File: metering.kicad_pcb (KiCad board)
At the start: 2 copper layers, 75 x 86 mm, 61 parts, among them J1 Conn_01x08, J2 USB_C_Receptacle_USB2.0_16P, J3 Prog, P1 Conn_01x08, SW1 Reset, SW2 Boot, U1 USBLC6-2SC6, U2 AMS1117-3.3, U3 ESP32-C3-WROOM-02U, U4 74HC14, X1 Screw_Terminal_01x06, X2 Screw_Terminal_01x06, Y1 32.768kHz

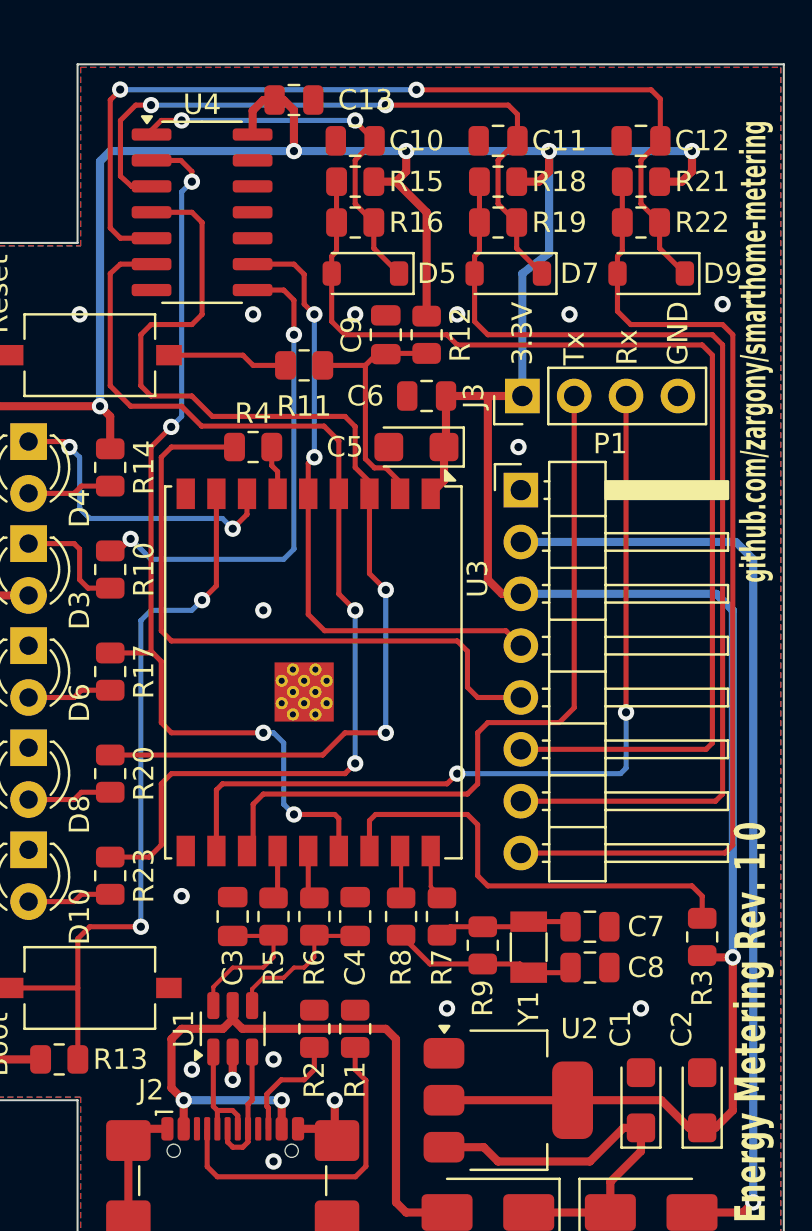
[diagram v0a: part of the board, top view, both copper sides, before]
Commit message: Add more GND vias
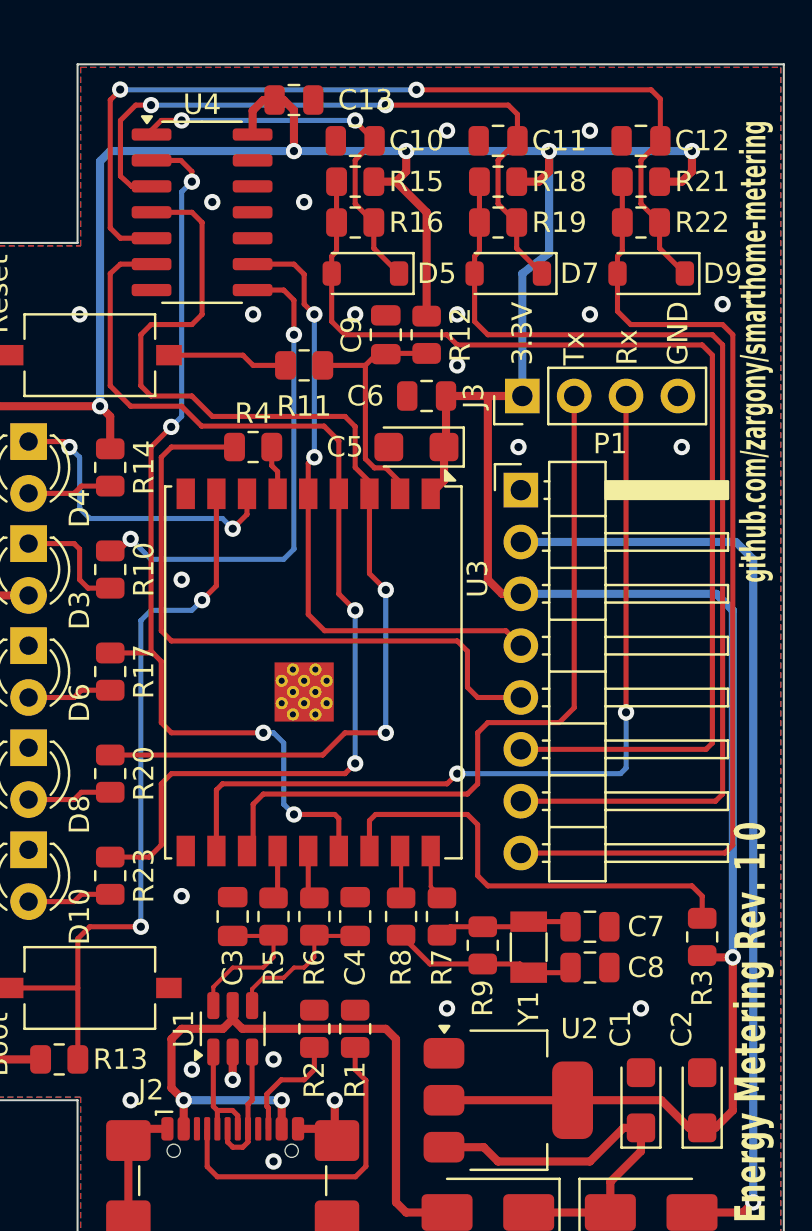
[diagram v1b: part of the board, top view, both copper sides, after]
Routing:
- net GND: vias 16 -> 23
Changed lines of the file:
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@@
+	)
+	(via
+		(at 49.5 121)
+		(size 0.8)
+		(drill 0.4)
+		(layers "F.Cu" "B.Cu")
+		(free yes)
+		(net 1)
+	)
+	(via
+		(at 65.5 85)
+		(size 0.8)
+		(drill 0.4)
+		(layers "F.Cu" "B.Cu")
+		(free yes)
+		(net 1)
 	)
 	(via
@@
 	)
 	(via
+		(at 65 73.5)
+		(size 0.8)
+		(drill 0.4)
+		(layers "F.Cu" "B.Cu")
+		(free yes)
+		(net 1)
+	)
+	(via
 		(at 52.5 119.5)
+		(size 0.8)
+		(drill 0.4)
+		(layers "F.Cu" "B.Cu")
+		(free yes)
+		(net 1)
+	)
+	(via
+		(at 53.5 77)
 		(size 0.8)
 		(drill 0.4)
@@
 	)
 	(via
-		(at 56 97)
+		(at 52 95.5)
 		(size 0.8)
 		(drill 0.4)
@@
 	)
 	(via
-		(at 71 82.5)
+		(at 72 82.5)
+		(size 0.8)
+		(drill 0.4)
+		(layers "F.Cu" "B.Cu")
+		(free yes)
+		(net 1)
+	)
+	(via
+		(at 58 77)
 		(size 0.8)
 		(drill 0.4)
@@
 	(via
 		(at 65 116.5)
+		(size 0.8)
+		(drill 0.4)
+		(layers "F.Cu" "B.Cu")
+		(free yes)
+		(net 1)
+	)
+	(via
+		(at 72 73.5)
 		(size 0.8)
 		(drill 0.4)
@@
 		(size 0.8)
 		(drill 0.4)
+		(layers "F.Cu" "B.Cu")
+		(free yes)
+		(net 1)
+	)
+	(via
+		(at 76.5 89)
+		(size 0.8)
+		(drill 0.4)

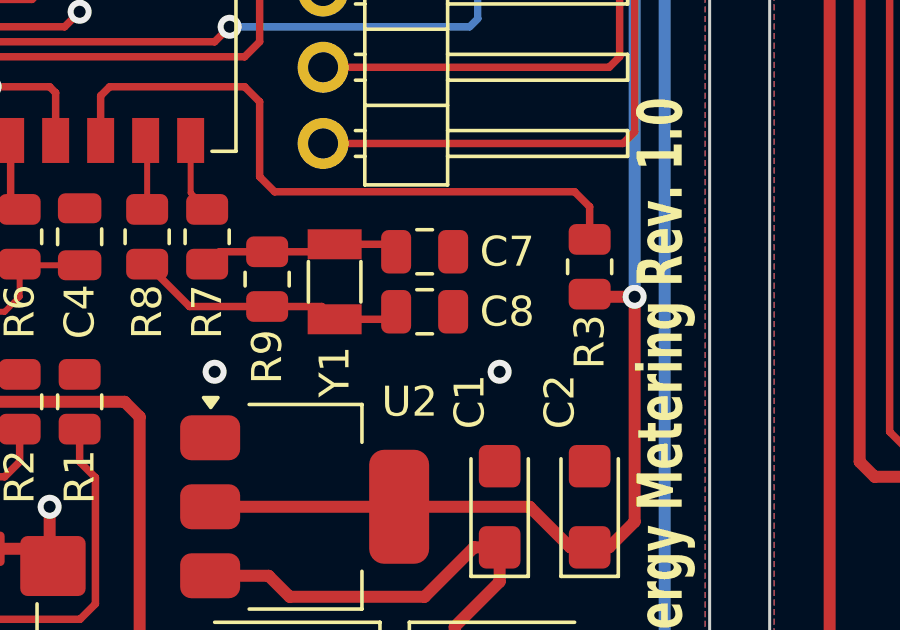
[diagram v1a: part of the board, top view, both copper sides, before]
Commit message: Fix pcb manufacturing warnings
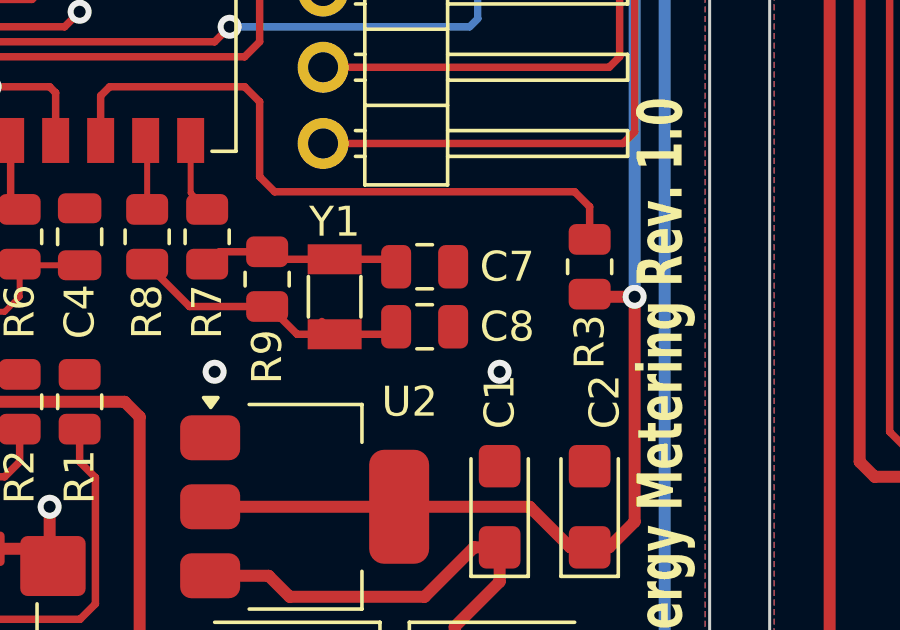
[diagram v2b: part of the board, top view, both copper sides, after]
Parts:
- moved C7 0.50 mm to (72.0, 113.0)
- moved C8 0.50 mm to (72.0, 115.0)
- moved Y1 0.50 mm to (69.0, 114.0)
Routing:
- net Net-(C8-Pad1): track 9.16 -> 9.97 mm
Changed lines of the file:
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@@
 		(tags "capacitor tantalum")
 		(property "Reference" "C1"
-			(at 3.5 -1 90)
+			(at 3.5 0 90)
 			(layer "F.SilkS")
 			(effects
@@
 	(footprint "Capacitor_SMD:C_0805_2012Metric"
 		(layer "F.Cu")
-		(at 72 114.5)
+		(at 72 115)
 		(descr "Capacitor SMD 0805 (2012 Metric), square (rectangular) end terminal, IPC-7351 nominal, (Body size source: IPC-SM-782 page 76, https://www.pcb-3d.com/wordpress/wp-content/uploads/ipc-sm-782a_amendment_1_and_2.pdf, https://docs.google.com/spreadsheets/d/1BsfQQcO9C6DZCsRaXUlFlo91Tg2WpOkGARC1WS5S8t0/edit?usp=sharing), generated with kicad-footprint-generator")
 		(tags "capacitor")
@@
 	(footprint "Capacitor_SMD:C_0805_2012Metric"
 		(layer "F.Cu")
-		(at 72 112.5)
+		(at 72 113)
 		(descr "Capacitor SMD 0805 (2012 Metric), square (rectangular) end terminal, IPC-7351 nominal, (Body size source: IPC-SM-782 page 76, https://www.pcb-3d.com/wordpress/wp-content/uploads/ipc-sm-782a_amendment_1_and_2.pdf, https://docs.google.com/spreadsheets/d/1BsfQQcO9C6DZCsRaXUlFlo91Tg2WpOkGARC1WS5S8t0/edit?usp=sharing), generated with kicad-footprint-generator")
 		(tags "capacitor")
@@
 		(tags "capacitor tantalum")
 		(property "Reference" "C2"
-			(at 3.5 -1 90)
+			(at 3.5 0.5 90)
 			(layer "F.SilkS")
 			(effects
@@
 	(footprint "Crystal:Crystal_SMD_3215-2Pin_3.2x1.5mm"
 		(layer "F.Cu")
-		(at 69 113.5 -90)
+		(at 69 114 -90)
 		(descr "SMD Crystal FC-135 https://support.epson.biz/td/api/doc_check.php?dl=brief_FC-135R_en.pdf")
 		(tags "SMD SMT Crystal")
 		(property "Reference" "Y1"
-			(at 3 0 90)
+			(at -2.5 0 180)
 			(layer "F.SilkS")
 			(effects
@@
 	)
 	(segment
-		(start 71.05 114.5)
-		(end 70.8 114.75)
+		(start 71.05 115)
+		(end 70.8 115.25)
 		(width 0.25)
 		(layer "F.Cu")
@@
 	)
 	(segment
-		(start 69 114.75)
-		(end 68.575 114.325)
+		(start 69 115.25)
+		(end 68.575 114.825)
 		(width 0.25)
 		(layer "F.Cu")
@@
 	)
 	(segment
-		(start 68.575 114.325)
-		(end 66.75 114.325)
+		(start 66.825 114.325)
+		(end 67.75 115.25)
+		(width 0.25)
+		(layer "F.Cu")
+		(net 12)
+	)
+	(segment
+		(start 66.75 114.325)
+		(end 66.825 114.325)
 		(width 0.25)
 		(layer "F.Cu")
@@
 	)
 	(segment
-		(start 70.8 114.75)
-		(end 69 114.75)
+		(start 67.75 115.25)
+		(end 69 115.25)
 		(width 0.25)
 		(layer "F.Cu")
@@
 	)
 	(segment
-		(start 69 112.25)
-		(end 68.75 112.5)
+		(start 70.8 115.25)
+		(end 69 115.25)
+		(width 0.25)
+		(layer "F.Cu")
+		(net 12)
+	)
+	(segment
+		(start 69 112.75)
+		(end 68.75 113)
 		(width 0.25)
 		(layer "F.Cu")
@@
 	)
 	(segment
-		(start 71.05 112.5)
-		(end 70.8 112.25)
+		(start 71.05 113)
+		(end 70.8 112.75)
+		(width 0.25)
+		(layer "F.Cu")
+		(net 13)
+	)
+	(segment
+		(start 66.75 112.5)
+		(end 67 112.75)
 		(width 0.25)
 		(layer "F.Cu")
@@
 	)
 	(segment
-		(start 68.75 112.5)
-		(end 66.75 112.5)
+		(start 70.8 112.75)
+		(end 69 112.75)
 		(width 0.25)
 		(layer "F.Cu")
@@
 	)
 	(segment
-		(start 70.8 112.25)
-		(end 69 112.25)
+		(start 67 112.75)
+		(end 69 112.75)
 		(width 0.25)
 		(layer "F.Cu")

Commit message: Release 1.1
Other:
- board text added: "Energy Metering ${REVISION}"
- board text removed: "Energy Metering Rev. ${REVISION}"
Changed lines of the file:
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@@
 	(title_block
 		(title "Smart Home Energy Metering")
-		(date "2025-06-27")
-		(rev "1.0")
+		(date "2025-06-30")
+		(rev "1.1")
 		(comment 1 "https://github.com/zargony/smarthome-metering")
 		(comment 2 "PCB for Camdenboss CNMB-2-2 DIN rail enclosure")
@@
 		)
 	)
-	(gr_text "Energy Metering Rev. ${REVISION}"
+	(gr_text "Energy Metering ${REVISION}"
 		(at 80.75 127 90)
 		(layer "F.SilkS")
